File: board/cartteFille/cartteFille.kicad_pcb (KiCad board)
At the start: 2 copper layers, 80 x 100 mm, 65 parts, among them U1 LM358, U20 MCP23018-E/SS, U21-2 SN74LVC2G14DBVTG4, U23-4 SN74LVC2G14DBVTG4, U25-6 SN74LVC2G14DBVTG4, U27-8 SN74LVC2G14DBVTG4

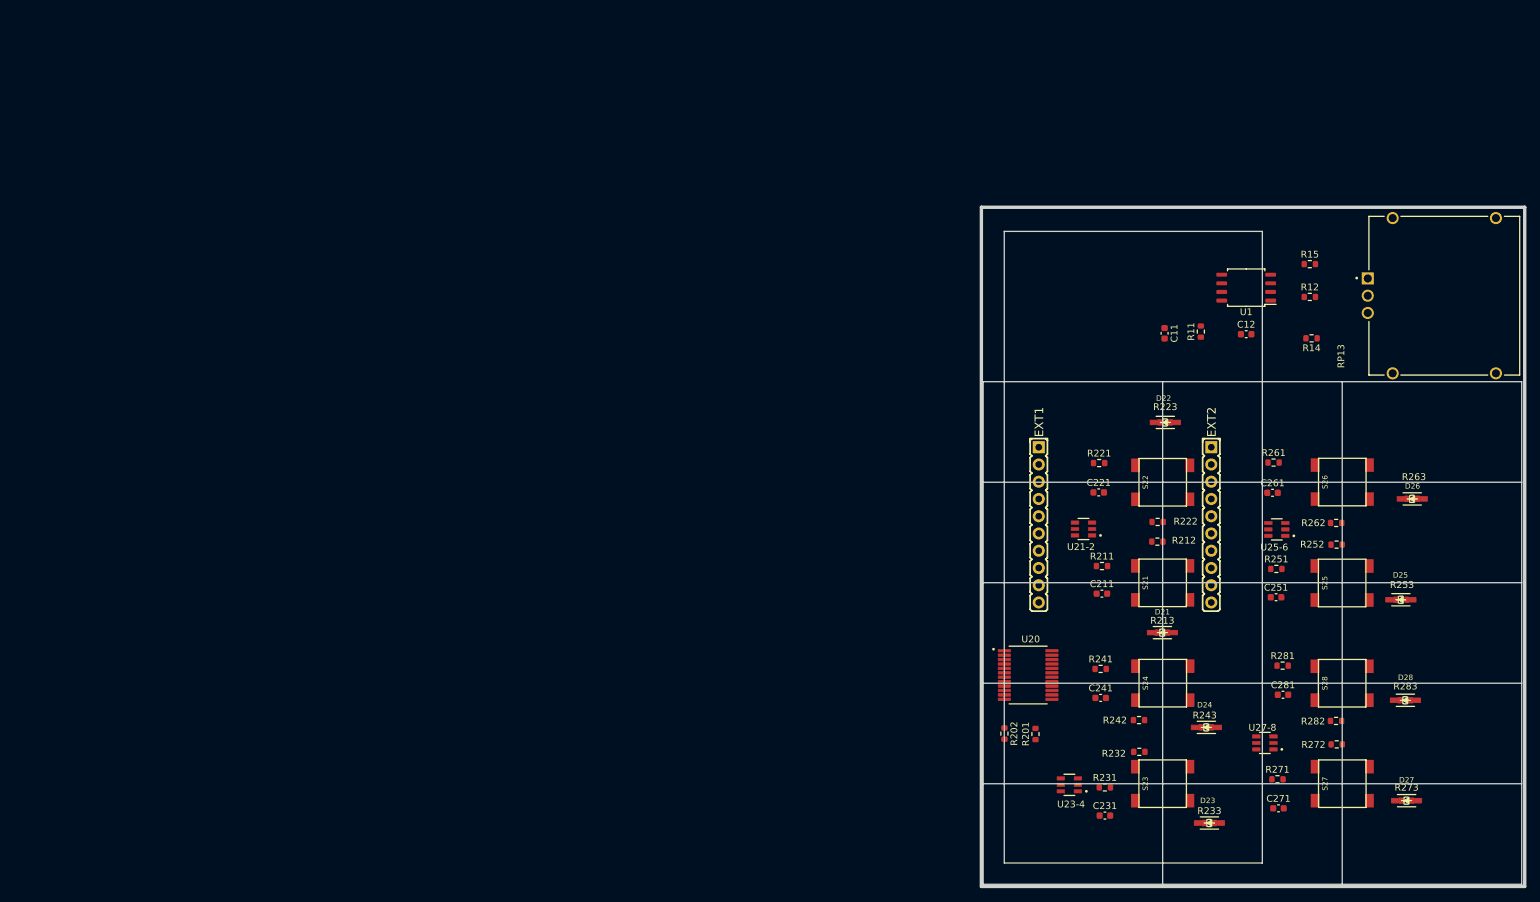
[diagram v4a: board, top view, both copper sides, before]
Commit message: Boutton_spec_mecha_1_incomplete
premier placement avant intégration du potentiomètre suite a la réception de la vue mécanique sans potentiomètre
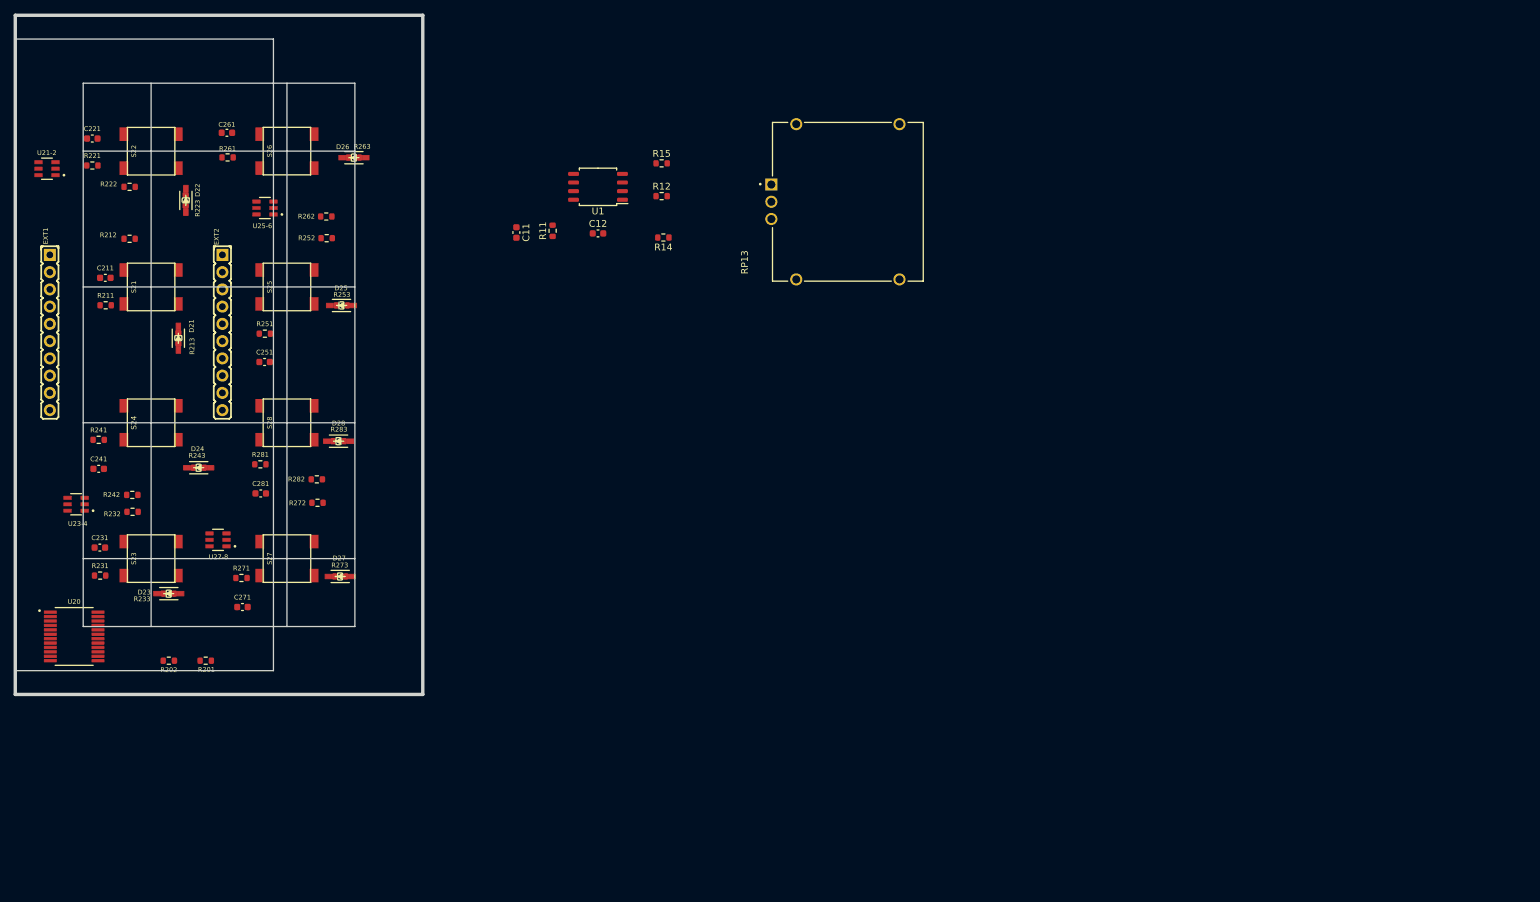
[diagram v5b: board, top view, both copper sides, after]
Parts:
- moved D26 163.7 mm to (49.9, 21.0)
- moved R263 163.7 mm to (49.9, 20.9)
- moved S26 162.9 mm to (40.0, 20.0)
- moved C261 162.8 mm to (31.2, 17.3)
- moved R253 161.9 mm to (48.1, 42.7)
- moved D25 161.9 mm to (48.0, 42.7)
- moved D28 161.6 mm to (47.6, 62.7)
- moved R283 161.6 mm to (47.6, 62.7)
- moved U21-2 161.6 mm to (4.67, 22.6)
- moved S25 161.4 mm to (40.0, 40.0)
- moved D27 160.5 mm to (47.8, 82.6)
- moved R273 160.5 mm to (47.8, 82.6)
- moved R261 160.4 mm to (31.3, 20.9)
- moved S28 160.0 mm to (40.0, 60.0)
- moved R222 159.2 mm to (16.8, 25.3)
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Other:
- board size 80 x 100 mm -> 60 x 100 mm

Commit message: remote_potentiometer_without_pinheader
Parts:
- moved R12 72.6 mm to (25.6, 5.67)
- moved R11 72.2 mm to (9.80, 11.6), turned to -90 degrees
- moved U1 70.3 mm to (18.1, 6.17)
- moved C12 68.1 mm to (20.9, 11.4)
- moved R14 67.4 mm to (32.3, 9.15)
- moved R15 66.2 mm to (32.0, 2.30)
- moved C11 63.3 mm to (13.8, 11.7), turned to 90 degrees
- moved RP13 14.6 mm to (117.7, 13.7)
- moved U20 2.86 mm to (11.4, 92.2)
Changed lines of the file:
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@@
   )
   (footprint "Resistor_SMD:R_0603_1608Metric" (layer "F.Cu")
-    (at 95.17 26.628)
+    (at 25.63 5.665)
     (descr "Resistor SMD 0603 (1608 Metric), square (rectangular) end terminal, IPC_7351 nominal, (Body size source: IPC-SM-782 page 72, https://www.pcb-3d.com/wordpress/wp-content/uploads/ipc-sm-782a_amendment_1_and_2.pdf), generated with kicad-footprint-generator")
     (tags "resistor")
@@
     (attr smd)
     (fp_text reference "R12" (at 0 -1.43) (layer "F.SilkS")
-      (effects (font (size 1 1) (thickness 0.15)))
+      (effects (font (size 0.7 0.7) (thickness 0.15)))
     )
     (fp_text value "150Ohm" (at 0 1.43) (layer "F.Fab")
-      (effects (font (size 1 1) (thickness 0.15)))
+      (effects (font (size 0.7 0.7) (thickness 0.15)))
     )
     (fp_text user "${REFERENCE}" (at 0 0) (layer "F.Fab")
@@
       (effects (font (size 0.7 0.7) (thickness 0.15)))
     )
-    (fp_text value "150Ohm" (at 0 2.032) (layer "F.Fab")
+    (fp_text value "150Ohm" (at 0.105 1.76) (layer "F.Fab")
       (effects (font (size 0.7 0.7) (thickness 0.15)))
     )
@@
   )
   (footprint "Resistor_SMD:R_0603_1608Metric" (layer "F.Cu")
-    (at 95.17 21.802)
+    (at 31.955 2.3)
     (descr "Resistor SMD 0603 (1608 Metric), square (rectangular) end terminal, IPC_7351 nominal, (Body size source: IPC-SM-782 page 72, https://www.pcb-3d.com/wordpress/wp-content/uploads/ipc-sm-782a_amendment_1_and_2.pdf), generated with kicad-footprint-generator")
     (tags "resistor")
@@
     (attr smd)
     (fp_text reference "R15" (at 0 -1.43) (layer "F.SilkS")
-      (effects (font (size 1 1) (thickness 0.15)))
+      (effects (font (size 0.7 0.7) (thickness 0.15)))
     )
     (fp_text value "3.9kOhm" (at 0 1.43) (layer "F.Fab")
-      (effects (font (size 1 1) (thickness 0.15)))
+      (effects (font (size 0.7 0.7) (thickness 0.15)))
     )
     (fp_text user "${REFERENCE}" (at 0 0) (layer "F.Fab")
@@
   )
   (footprint "MCP23018-E_SS:SOP65P780X200-24N" (layer "F.Cu")
-    (at 8.67 91.46)
+    (at 11.4225 92.24)
     (property "MANUFACTURER" "Microchip")
     (property "PARTREV" "N/A")
@@
       (effects (font (size 0.7 0.7) (thickness 0.15)))
     )
-    (fp_text value "MCP23018-E/SS" (at 0.056 5.309) (layer "F.Fab")
+    (fp_text value "MCP23018-E/SS" (at -0.0825 5.02) (layer "F.Fab")
       (effects (font (size 0.7 0.7) (thickness 0.15)))
     )
@@
   )
   (footprint "Package_SO:SOIC-8_5.275x5.275mm_P1.27mm" (layer "F.Cu")
-    (at 85.8 25.26 180)
+    (at 18.11 6.165 180)
     (descr "SOIC, 8 Pin (http://ww1.microchip.com/downloads/en/DeviceDoc/20005045C.pdf#page=23), generated with kicad-footprint-generator ipc_gullwing_generator.py")
     (tags "SOIC SO")
@@
     (attr smd)
     (fp_text reference "U1" (at 0 -3.59) (layer "F.SilkS")
-      (effects (font (size 1 1) (thickness 0.15)))
+      (effects (font (size 0.7 0.7) (thickness 0.15)))
     )
     (fp_text value "LM358" (at 0 3.59) (layer "F.Fab")
-      (effects (font (size 1 1) (thickness 0.15)))
-    )
-    (fp_text user "${REFERENCE}" (at 0 0) (layer "F.Fab")
-      (effects (font (size 1 1) (thickness 0.15)))
+      (effects (font (size 0.7 0.7) (thickness 0.15)))
+    )
+    (fp_text user "${REFERENCE}" (at 0 0) (layer "F.Fab")
+      (effects (font (size 0.7 0.7) (thickness 0.15)))
     )
     (fp_line (start 0 2.7475) (end 2.7475 2.7475) (layer "F.SilkS") (width 0.12))
@@
   )
   (footprint "Capacitor_SMD:C_0603_1608Metric" (layer "F.Cu")
-    (at 85.8 32.118)
+    (at 20.91 11.45)
     (descr "Capacitor SMD 0603 (1608 Metric), square (rectangular) end terminal, IPC_7351 nominal, (Body size source: IPC-SM-782 page 76, https://www.pcb-3d.com/wordpress/wp-content/uploads/ipc-sm-782a_amendment_1_and_2.pdf), generated with kicad-footprint-generator")
     (tags "capacitor")
@@
     (attr smd)
     (fp_text reference "C12" (at 0 -1.43) (layer "F.SilkS")
-      (effects (font (size 1 1) (thickness 0.15)))
+      (effects (font (size 0.7 0.7) (thickness 0.15)))
     )
     (fp_text value "100nF" (at 0 1.43) (layer "F.Fab")
-      (effects (font (size 1 1) (thickness 0.15)))
+      (effects (font (size 0.7 0.7) (thickness 0.15)))
     )
     (fp_text user "${REFERENCE}" (at 0 0) (layer "F.Fab")
@@
       (effects (font (size 0.7 0.7) (thickness 0.15)))
     )
-    (fp_text value "NSI45020T1G" (at 0.254 3.302) (layer "F.Fab")
+    (fp_text value "NSI45020T1G" (at 0.025 2.85) (layer "F.Fab")
       (effects (font (size 0.7 0.7) (thickness 0.15)))
     )
@@
   )
   (footprint "Resistor_SMD:R_0603_1608Metric" (layer "F.Cu")
-    (at 79.12 31.73 90)
+    (at 9.8 11.645 -90)
     (descr "Resistor SMD 0603 (1608 Metric), square (rectangular) end terminal, IPC_7351 nominal, (Body size source: IPC-SM-782 page 72, https://www.pcb-3d.com/wordpress/wp-content/uploads/ipc-sm-782a_amendment_1_and_2.pdf), generated with kicad-footprint-generator")
     (tags "resistor")
@@
     (attr smd)
     (fp_text reference "R11" (at 0 -1.43 90) (layer "F.SilkS")
-      (effects (font (size 1 1) (thickness 0.15)))
+      (effects (font (size 0.7 0.7) (thickness 0.15)))
     )
     (fp_text value "10KOhm" (at 0 1.43 90) (layer "F.Fab")
-      (effects (font (size 1 1) (thickness 0.15)))
+      (effects (font (size 0.7 0.7) (thickness 0.15)))
     )
     (fp_text user "${REFERENCE}" (at 0 0 90) (layer "F.Fab")
@@
     (fp_line (start 0.8 0.4125) (end -0.8 0.4125) (layer "F.Fab") (width 0.1))
     (fp_line (start 0.8 -0.4125) (end 0.8 0.4125) (layer "F.Fab") (width 0.1))
-    (pad "1" smd roundrect (at -0.825 0 90) (size 0.8 0.95) (layers "F.Cu" "F.Paste" "F.Mask") (roundrect_rratio 0.25)
+    (pad "1" smd roundrect (at -0.825 0 270) (size 0.8 0.95) (layers "F.Cu" "F.Paste" "F.Mask") (roundrect_rratio 0.25)
       (net 2 "GND") (pintype "passive"))
-    (pad "2" smd roundrect (at 0.825 0 90) (size 0.8 0.95) (layers "F.Cu" "F.Paste" "F.Mask") (roundrect_rratio 0.25)
+    (pad "2" smd roundrect (at 0.825 0 270) (size 0.8 0.95) (layers "F.Cu" "F.Paste" "F.Mask") (roundrect_rratio 0.25)
       (net 1 "/ADC_CH0-U11RP1") (pintype "passive"))
     (model "${KICAD6_3DMODEL_DIR}/Resistor_SMD.3dshapes/R_0603_1608Metric.wrl"
@@
   )
   (footprint "PCW1J-R24-BAB103L:TRIM_PCW1J-R24-BAB103L" (layer "F.Cu")
-    (at 122.5925 27.46 -90)
+    (at 117.67 13.7 -90)
     (property "MANUFACTURER" "Bourns")
     (property "MAXIMUM_PACKAGE_HIEGHT" "32.31mm")
@@
   )
   (footprint "Capacitor_SMD:C_0603_1608Metric" (layer "F.Cu")
-    (at 73.786 31.984 -90)
+    (at 13.81 11.655 90)
     (descr "Capacitor SMD 0603 (1608 Metric), square (rectangular) end terminal, IPC_7351 nominal, (Body size source: IPC-SM-782 page 76, https://www.pcb-3d.com/wordpress/wp-content/uploads/ipc-sm-782a_amendment_1_and_2.pdf), generated with kicad-footprint-generator")
     (tags "capacitor")
@@
     (property "Sheetname" "")
     (attr smd)
-    (fp_text reference "C11" (at 0 -1.43 90) (layer "F.SilkS")
-      (effects (font (size 1 1) (thickness 0.15)))
+    (fp_text reference "C11" (at -0.02 -1.423 90) (layer "F.SilkS")
+      (effects (font (size 0.7 0.7) (thickness 0.15)))
     )
     (fp_text value "100nF" (at 0 1.43 90) (layer "F.Fab")
-      (effects (font (size 1 1) (thickness 0.15)))
+      (effects (font (size 0.7 0.7) (thickness 0.15)))
     )
     (fp_text user "${REFERENCE}" (at 0 0 90) (layer "F.Fab")
@@
     (fp_line (start -0.8 -0.4) (end 0.8 -0.4) (layer "F.Fab") (width 0.1))
     (fp_line (start 0.8 0.4) (end -0.8 0.4) (layer "F.Fab") (width 0.1))
-    (pad "1" smd roundrect (at -0.775 0 270) (size 0.9 0.95) (layers "F.Cu" "F.Paste" "F.Mask") (roundrect_rratio 0.25)
+    (pad "1" smd roundrect (at -0.775 0 90) (size 0.9 0.95) (layers "F.Cu" "F.Paste" "F.Mask") (roundrect_rratio 0.25)
       (net 1 "/ADC_CH0-U11RP1") (pintype "passive"))
-    (pad "2" smd roundrect (at 0.775 0 270) (size 0.9 0.95) (layers "F.Cu" "F.Paste" "F.Mask") (roundrect_rratio 0.25)
+    (pad "2" smd roundrect (at 0.775 0 90) (size 0.9 0.95) (layers "F.Cu" "F.Paste" "F.Mask") (roundrect_rratio 0.25)
       (net 2 "GND") (pintype "passive"))
     (model "${KICAD6_3DMODEL_DIR}/Capacitor_SMD.3dshapes/C_0603_1608Metric.wrl"
@@
   )
   (footprint "Resistor_SMD:R_0603_1608Metric" (layer "F.Cu")
-    (at 95.424 32.724 180)
+    (at 32.27 9.15 180)
     (descr "Resistor SMD 0603 (1608 Metric), square (rectangular) end terminal, IPC_7351 nominal, (Body size source: IPC-SM-782 page 72, https://www.pcb-3d.com/wordpress/wp-content/uploads/ipc-sm-782a_amendment_1_and_2.pdf), generated with kicad-footprint-generator")
     (tags "resistor")
@@
     (attr smd)
     (fp_text reference "R14" (at 0 -1.43) (layer "F.SilkS")
-      (effects (font (size 1 1) (thickness 0.15)))
+      (effects (font (size 0.7 0.7) (thickness 0.15)))
     )
     (fp_text value "680Ohm" (at 0 1.43) (layer "F.Fab")
-      (effects (font (size 1 1) (thickness 0.15)))
-    )
-    (fp_text user "${REFERENCE}" (at 0 0) (layer "F.Fab")
+      (effects (font (size 0.7 0.7) (thickness 0.15)))
+    )
+    (fp_text user "${REFERENCE}" (at 0 0) (layer "F.Fab")
